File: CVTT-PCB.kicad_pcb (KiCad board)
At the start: 4 copper layers, 66 x 88 mm, 69 parts, among them J1 SERVO1, J2 SERVO2, J3 LCD SCREEN, J4 LCD BUTTONS, J5 Conn_ARM_SWD_TagConnect_TC2030, J7 Barrel_Jack, P2 DC2, P5 DC1, P8 STEPPER, Q7 BSS138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

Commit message: update layout
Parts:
- U7: value RASPBERRY_PI_ZERO_2_W -> RASPBERRY PI ZERO 2 W
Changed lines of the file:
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@@
 			)
 		)
-		(property "Value" "RASPBERRY_PI_ZERO_2_W"
+		(property "Value" "RASPBERRY PI ZERO 2 W"
 			(at 18.8 -16.4 0)
 			(layer "F.SilkS")
@@
 			(offset
 				(xyz 13.5 0 6.5)
-			)
-			(scale
-				(xyz 1 1 1)
-			)
-			(rotate
-				(xyz -90 -0 -0)
-			)
-		)
-		(model "/Users/michaeljao/Downloads/PJ-002B.step"
-			(offset
-				(xyz 13.5 0 6.5)

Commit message: update layout
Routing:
- net GND: track 43.2 -> 46.4 mm

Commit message: update layout labeling
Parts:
- removed the REF** at (168.5, 137.0)
- removed the REF** at (109.5, 137.0)
- added REF**: MountingHole_2.7mm_M2.5_DIN965_Pad, MountingHole:MountingHole_2.7mm_M2.5_DIN965_Pad, F.Cu at (109.5, 137.0)
- added REF**: MountingHole_2.7mm_M2.5_DIN965_Pad, MountingHole:MountingHole_2.7mm_M2.5_DIN965_Pad, F.Cu at (168.5, 137.0)
- U7: value RASPBERRY PI ZERO 2 W -> RASPBERRY_PI_ZERO_2_W
- moved R11 2.51 mm to (124.3, 101.8)
- moved R12 1.75 mm to (122.7, 103.9), turned to -90 degrees
- moved J4 1.51 mm to (118.5, 94.7)
- moved R10 1.03 mm to (122.7, 99.1)
- moved R19 0.64 mm to (133.9, 93.0)
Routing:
- net /LCD_BUTTONU: track 19.2 -> 17.7 mm
- net /LCD_BUTTONC: track 17.3 -> 15.8 mm
- net /LCD_BUTTOND: track 17.1 -> 15.6 mm
- net /DRV_EN: track 105.9 -> 106.6 mm
- net /SERVO1_PWM: track 30.3 -> 29.8 mm
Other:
- outline, holes or cut-outs redrawn
- board text added: "D C U"
- board text added: "VIN GND CK MI MO CS R D/C BL"

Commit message: update assets
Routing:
- net GND: vias 86 -> 87

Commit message: update layout
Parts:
- U7: value RASPBERRY_PI_ZERO_2_W -> RASPBERRY PI ZERO 2 W
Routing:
- net +3.3V: track 229.0 -> 220.3 mm
- net GND: track 46.4 -> 47.3 mm, vias 87 -> 86

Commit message: update assets
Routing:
- net GND: track 47.3 -> 49.1 mm, vias 86 -> 88

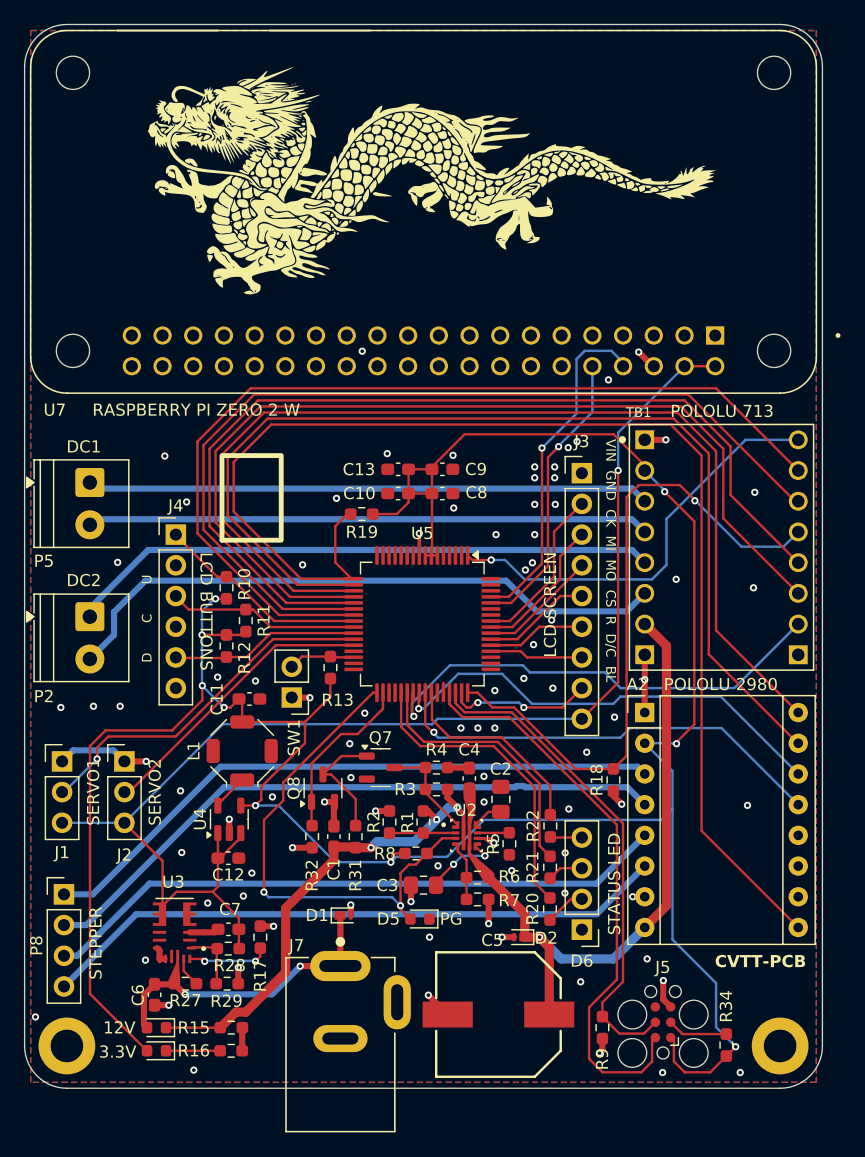
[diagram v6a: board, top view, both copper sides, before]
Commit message: fix MPM3610GQV-P resistors
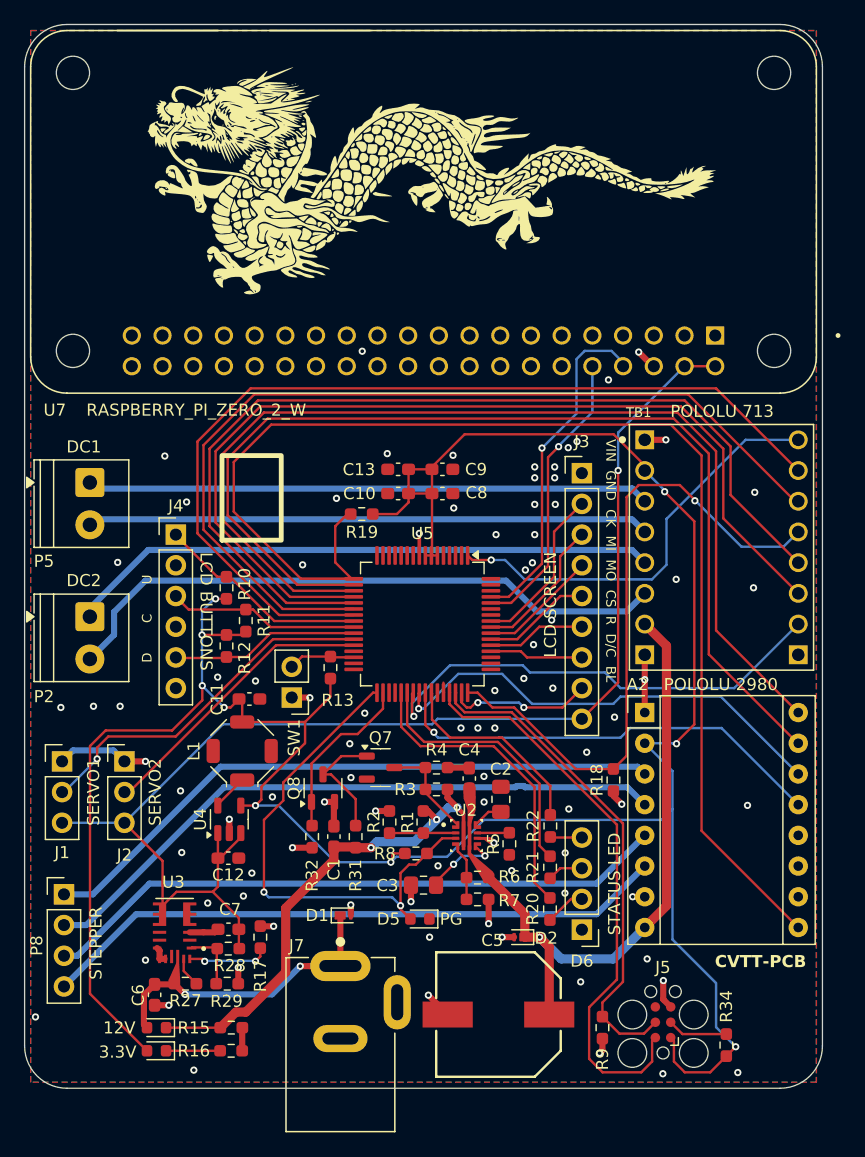
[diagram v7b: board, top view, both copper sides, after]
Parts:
- removed REF** (x2): MountingHole_2.7mm_M2.5_DIN965_Pad, MountingHole:MountingHole_2.7mm_M2.5_DIN965_Pad
- R28: value 75k -> 270k
- R29: value 24k -> 51k
- U7: value RASPBERRY PI ZERO 2 W -> RASPBERRY_PI_ZERO_2_W
